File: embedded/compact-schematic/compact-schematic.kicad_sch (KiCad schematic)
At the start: 7 parts, among them Q1 NMOS, Q2 NMOS, Q3 NMOS

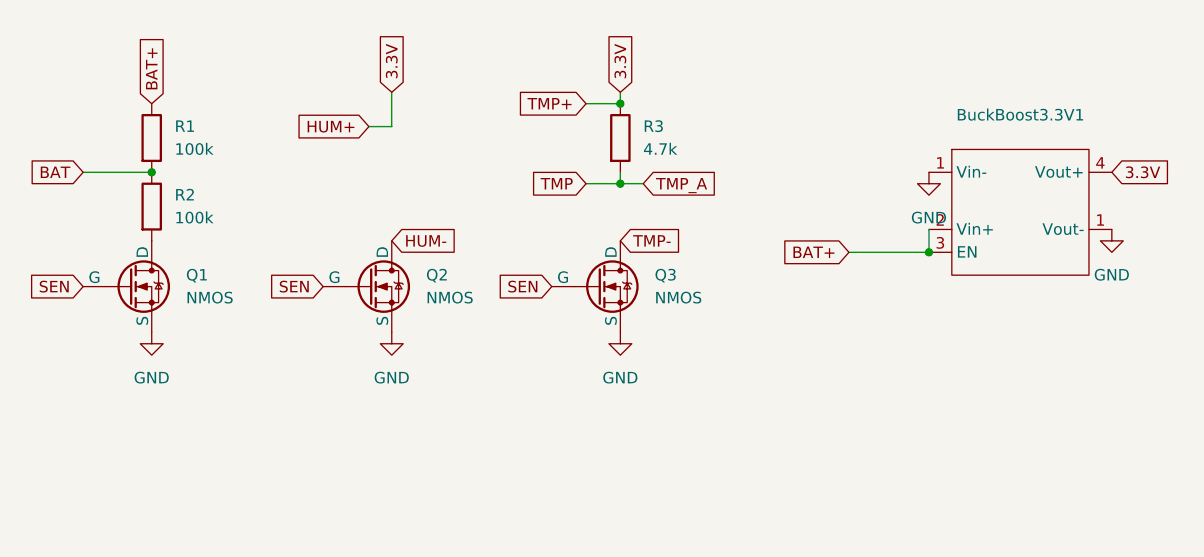
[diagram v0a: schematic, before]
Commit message: updated compact schematic
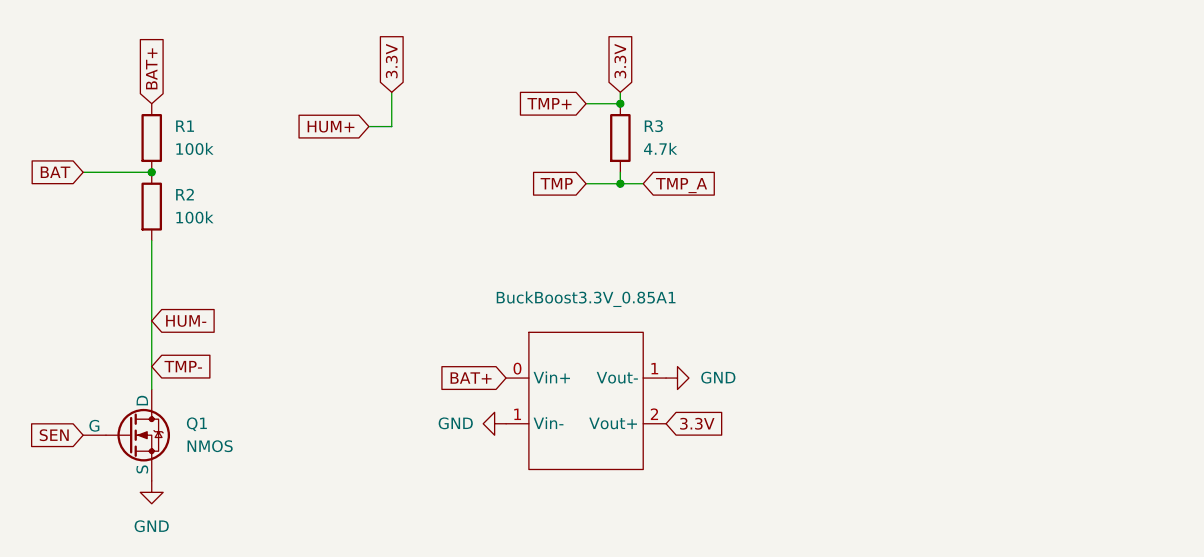
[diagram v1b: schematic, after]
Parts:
- removed BuckBoost3.3V1: ~, custom:BuckBoost3.3V, symbol custom:BuckBoost3.3V
- removed Q2, Q3: NMOS, Package_TO_SOT_SMD:SOT-23-3, symbol Simulation_SPICE:NMOS
- added BuckBoost3.3V_0.85A1: ~, custom:BuckBoost3.3V_0.85A, symbol custom:BuckBoost3.3V_0.85A
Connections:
- net 3.3V: now also BuckBoost3.3V_0.85A1.2 (Vout+)
- net BAT+: now also BuckBoost3.3V_0.85A1.0 (Vin+)
- net GND: now also BuckBoost3.3V_0.85A1.1 (Vout-)
- net HUM-: now also Q1.1 (D), R2.2
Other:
- moved on the sheet: Q1
